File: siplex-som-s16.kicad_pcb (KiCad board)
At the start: 8 copper layers, 30 x 30 mm, 58 parts, among them J1 RFShield_OnePiece, J2 Conn_01x20, J3 Conn_01x20, J4 Conn_01x20, J6 Conn_01x20, U1 STM32H743IIKx, U2 IS42S16160J-6BLI, U3 W25Q32JVZP, U4 AP2112K-3.3, U5 W25Q32JVZP, Y1 25MHz, Y2 32.768KHz

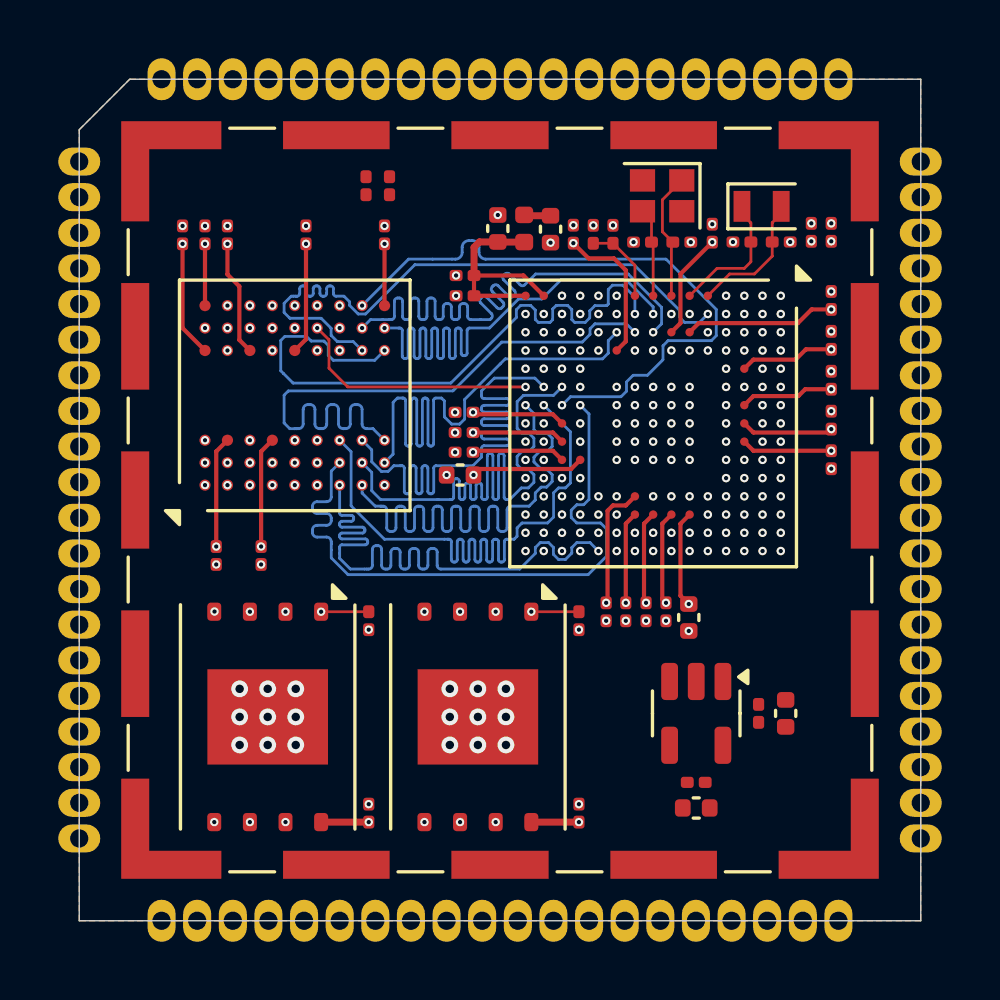
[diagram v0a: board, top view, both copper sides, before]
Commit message: Finished LTDC tracks
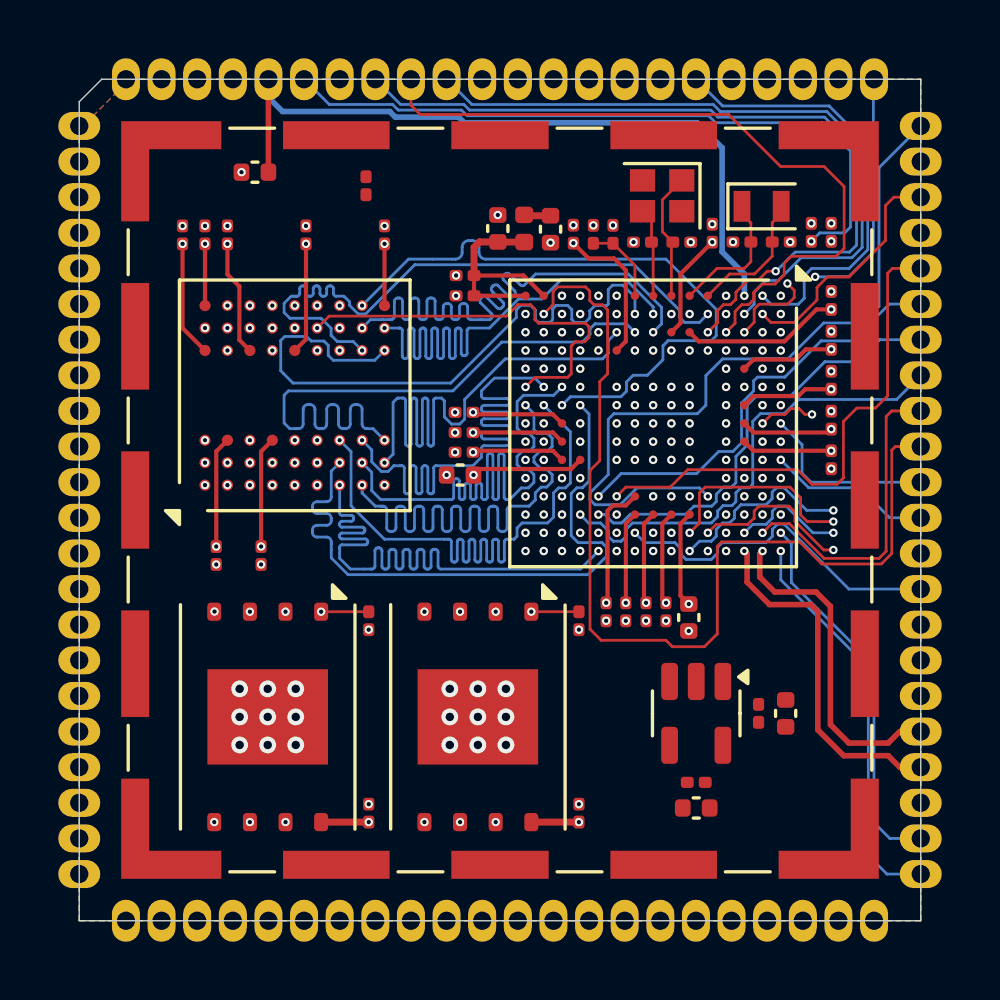
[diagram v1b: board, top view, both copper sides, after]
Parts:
- removed J2, J3, J4, J6: Conn_01x20, castellated_holes_header:castellated_01x20_P1.27mm
- added J5: Conn_01x22, castellated_holes_header:castellated_01x22_P1.27mm, F.Cu at (155.3, 111.4)
- added J7: Conn_01x22, castellated_holes_header:castellated_01x22_P1.27mm, F.Cu at (127.0, 83.1)
- added J8: Conn_01x22, castellated_holes_header:castellated_01x22_P1.27mm, F.Cu at (125.3, 84.7)
- added J9: Conn_01x22, castellated_holes_header:castellated_01x22_P1.27mm, F.Cu at (127.0, 113.1)
- C10: value 100n -> 10u; footprint Capacitor_SMD:C_0201_0603Metric -> Capacitor_SMD:C_0402_1005Metric
- moved C10 4.82 mm to (131.6, 86.4), turned to 180 degrees
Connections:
- C10 pad 1: GND -> VBAT
- C10 pad 2: +3V3 -> GND
- U1 pad A10: /MCU/SWO -> /Castellated_holes/SWO
- U1 pad A14: /MCU/SWCLK -> /Castellated_holes/SWCLK
- U1 pad A15: /MCU/SWDIO -> /Castellated_holes/SWDIO
- U1 pad A8: unconnected-(U1-PG13-PadA8) -> /Castellated_holes/LTDC_R0
- U1 pad A9: unconnected-(U1-PB4-PadA9) -> /Castellated_holes/SDMMC_IO3
- U1 pad B1: unconnected-(U1-PE4-PadB1) -> /Castellated_holes/LTDC_B0
- U1 pad B10: unconnected-(U1-PG10-PadB10) -> /Castellated_holes/LTDC_G3
- U1 pad B11: unconnected-(U1-PD6-PadB11) -> /Castellated_holes/SDMMC_CLK
- U1 pad B14: unconnected-(U1-PC10-PadB14) -> /Castellated_holes/LTDC_R2
- U1 pad B15: /MCU/USB_DP -> /Castellated_holes/USB_DP
- U1 pad B2: unconnected-(U1-PE5-PadB2) -> /Castellated_holes/LTDC_G0
- U1 pad B3: unconnected-(U1-PE6-PadB3) -> /Castellated_holes/LTDC_G1
- U1 pad B8: unconnected-(U1-PG12-PadB8) -> /Castellated_holes/LTDC_B1
- U1 pad B9: unconnected-(U1-PG11-PadB9) -> /Castellated_holes/SDMMC_IO2
- U1 pad C14: unconnected-(U1-PI2-PadC14) -> /Castellated_holes/LTDC_G7
- U1 pad C15: /MCU/USB_DN -> /Castellated_holes/USB_DN
- U1 pad C2: unconnected-(U1-PI7-PadC2) -> /Castellated_holes/LTDC_B7
- U1 pad C3: unconnected-(U1-PI6-PadC3) -> /Castellated_holes/LTDC_B6
- U1 pad C4: unconnected-(U1-PI5-PadC4) -> /Castellated_holes/LTDC_B5
- U1 pad D13: unconnected-(U1-PH15-PadD13) -> /Castellated_holes/LTDC_G4
- U1 pad D14: unconnected-(U1-PI1-PadD14) -> /Castellated_holes/LTDC_G6
- U1 pad D3: unconnected-(U1-PI9-PadD3) -> /Castellated_holes/LTDC_VSYNC
- U1 pad D4: unconnected-(U1-PI4-PadD4) -> /Castellated_holes/LTDC_B4
- U1 pad E12: unconnected-(U1-PH13-PadE12) -> /Castellated_holes/LTDC_G2
- U1 pad E14: unconnected-(U1-PI0-PadE14) -> /Castellated_holes/LTDC_G5
- U1 pad E15: /MCU/USB_VBUS_DET -> /Castellated_holes/USB_VBUS_DET
- U1 pad E3: unconnected-(U1-PI10-PadE3) -> /Castellated_holes/LTDC_HSYNC
- U1 pad F14: unconnected-(U1-PC9-PadF14) -> /Castellated_holes/LTDC_B2
- U1 pad F15: unconnected-(U1-PA8-PadF15) -> /Castellated_holes/LTDC_B3
- U1 pad J14: unconnected-(U1-PG7-PadJ14) -> /Castellated_holes/LTDC_CLK
- U1 pad J15: unconnected-(U1-PG6-PadJ15) -> /Castellated_holes/LTDC_R7
- U1 pad K12: unconnected-(U1-PH12-PadK12) -> /Castellated_holes/LTDC_R6
- U1 pad L1: unconnected-(U1-PF10-PadL1) -> /Castellated_holes/LTDC_DE
- U1 pad L12: unconnected-(U1-PH11-PadL12) -> /Castellated_holes/LTDC_R5
- U1 pad L13: unconnected-(U1-PH10-PadL13) -> /Castellated_holes/LTDC_R4
- U1 pad M13: unconnected-(U1-PH9-PadM13) -> /Castellated_holes/LTDC_R3
- U1 pad P2: unconnected-(U1-PA2-PadP2) -> /Castellated_holes/LTDC_R1
- U1 pad R14: unconnected-(U1-PB14-PadR14) -> /Castellated_holes/SDMMC_IO0
- U1 pad R15: unconnected-(U1-PB15-PadR15) -> /Castellated_holes/SDMMC_IO1
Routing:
- net /Castellated_holes/LTDC_R1: track 0.00 -> 34.8 mm, vias 0 -> 1
- net /Castellated_holes/LTDC_B2: track 0.00 -> 34.0 mm, vias 0 -> 2
- net /MCU/BOOT0: track 0.00 -> 32.7 mm
- net /Castellated_holes/LTDC_B3: track 0.00 -> 32.4 mm, vias 0 -> 2
- net /Castellated_holes/LTDC_HSYNC: track 0.00 -> 28.6 mm, vias 0 -> 2
- net /Castellated_holes/LTDC_G2: track 0.00 -> 26.8 mm, vias 0 -> 1
- net VBAT: track 0.00 -> 26.5 mm
- net /Castellated_holes/LTDC_VSYNC: track 0.00 -> 25.9 mm, vias 0 -> 1
- net /Castellated_holes/LTDC_G4: track 0.00 -> 25.1 mm, vias 0 -> 1
- net /Castellated_holes/LTDC_G5: track 0.00 -> 25.0 mm, vias 0 -> 2
- net /Castellated_holes/LTDC_B7: track 0.00 -> 24.8 mm, vias 0 -> 1
- net /Castellated_holes/LTDC_G7: track 0.00 -> 24.5 mm, vias 0 -> 2
- net /Castellated_holes/LTDC_G6: track 0.00 -> 23.7 mm, vias 0 -> 1
- net /Castellated_holes/LTDC_B5: track 0.00 -> 22.4 mm, vias 0 -> 1
- net /Castellated_holes/LTDC_B4: track 0.00 -> 22.2 mm, vias 0 -> 1
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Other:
- outline, holes or cut-outs redrawn

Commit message: test remote connection
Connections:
- U1 pad A11: unconnected-(U1-PD7-PadA11) -> /Castellated_holes/SDMMC_CMD
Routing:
- net unconnected-(U1-PE2-PadA2): track 0.00 -> 32.2 mm
- net unconnected-(U1-PE3-PadA1): track 0.00 -> 27.3 mm
- net /MCU/BOOT0: track 32.7 -> 34.0 mm
- net /Castellated_holes/LTDC_B0: track 16.0 -> 16.9 mm
- net /Castellated_holes/LTDC_B7: track 24.8 -> 25.8 mm
- net /Castellated_holes/LTDC_HSYNC: track 28.6 -> 29.5 mm
- net /Castellated_holes/LTDC_G1: track 10.5 -> 9.93 mm
- net unconnected-(U1-PD7-PadA11): vias 1 -> 0
- net /Castellated_holes/SDMMC_CMD: vias 0 -> 1
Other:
- board size 30 x 30 mm -> 31.6 x 31.6 mm

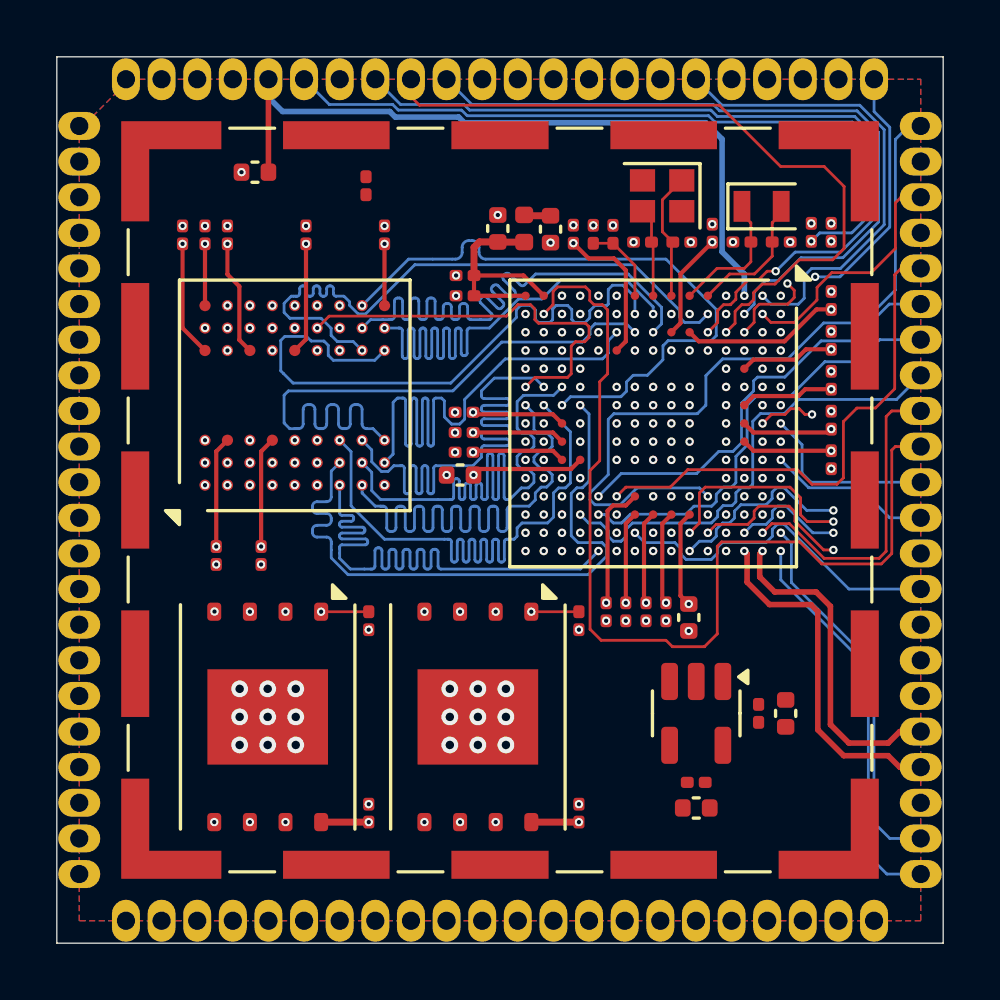
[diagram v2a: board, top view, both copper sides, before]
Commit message: Finished fanout all remaining pin, Power block left
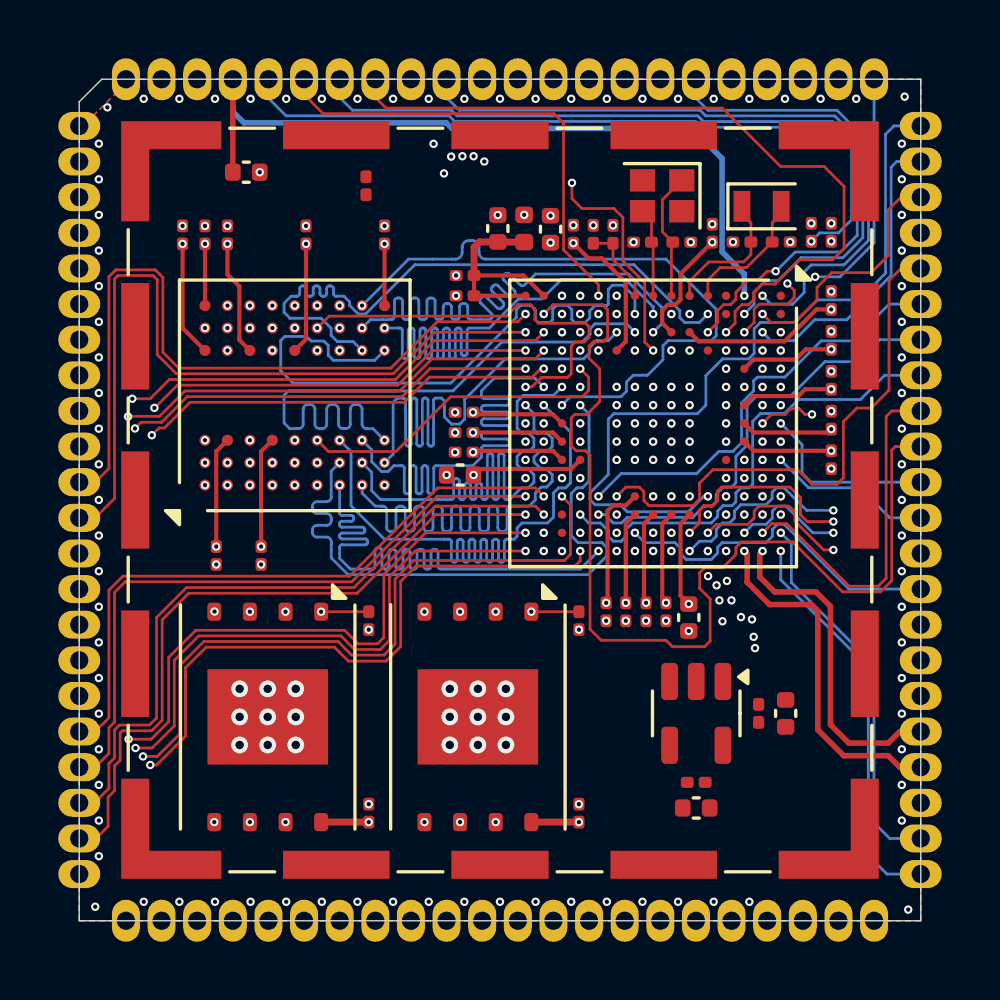
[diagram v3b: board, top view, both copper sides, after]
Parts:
- moved C10 0.31 mm to (131.3, 86.4), turned to 0 degrees
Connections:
- J7 pad 1: unconnected-(J7-Pin_1-Pad1) -> PB7
- J7 pad 2: unconnected-(J7-Pin_2-Pad2) -> PB5
- J7 pad 3: unconnected-(J7-Pin_3-Pad3) -> GND
- J7 pad 4: GND -> VBAT
- J7 pad 5: VBAT -> /MCU/BOOT0
- J7 pad 6: /MCU/BOOT0 -> /Castellated_holes/LTDC_DE
- J7 pad 7: /Castellated_holes/LTDC_DE -> /Castellated_holes/LTDC_HSYNC
- J7 pad 8: /Castellated_holes/LTDC_HSYNC -> /Castellated_holes/LTDC_VSYNC
- J7 pad 9: /Castellated_holes/LTDC_VSYNC -> GND
- J8 pad 1: unconnected-(J8-Pin_1-Pad1) -> PB8
- J8 pad 10: unconnected-(J8-Pin_10-Pad10) -> PA4
- J8 pad 11: unconnected-(J8-Pin_11-Pad11) -> PA3
- J8 pad 12: unconnected-(J8-Pin_12-Pad12) -> PA7
- J8 pad 13: unconnected-(J8-Pin_13-Pad13) -> PA6
- J8 pad 14: unconnected-(J8-Pin_14-Pad14) -> PA5
- J8 pad 15: unconnected-(J8-Pin_15-Pad15) -> PB0
- J8 pad 16: unconnected-(J8-Pin_16-Pad16) -> PB1
- J8 pad 17: unconnected-(J8-Pin_17-Pad17) -> PC5
- J8 pad 18: unconnected-(J8-Pin_18-Pad18) -> PB12
- J8 pad 19: unconnected-(J8-Pin_19-Pad19) -> PB10
- J8 pad 2: unconnected-(J8-Pin_2-Pad2) -> PB9
- J8 pad 20: unconnected-(J8-Pin_20-Pad20) -> PB13
- J8 pad 21: unconnected-(J8-Pin_21-Pad21) -> PB11
- J8 pad 22: unconnected-(J8-Pin_22-Pad22) -> PB14
- J8 pad 3: unconnected-(J8-Pin_3-Pad3) -> PH4
- J8 pad 4: unconnected-(J8-Pin_4-Pad4) -> GND
- J8 pad 5: unconnected-(J8-Pin_5-Pad5) -> PC0
- J8 pad 6: unconnected-(J8-Pin_6-Pad6) -> PC1
- J8 pad 7: unconnected-(J8-Pin_7-Pad7) -> PC4
- J8 pad 8: unconnected-(J8-Pin_8-Pad8) -> PA0
- J8 pad 9: unconnected-(J8-Pin_9-Pad9) -> PA1
- J9 pad 1: unconnected-(J9-Pin_1-Pad1) -> PB15
- J9 pad 10: unconnected-(J9-Pin_10-Pad10) -> PD3
- J9 pad 11: unconnected-(J9-Pin_11-Pad11) -> PD5
- J9 pad 12: unconnected-(J9-Pin_12-Pad12) -> PD6
- J9 pad 13: unconnected-(J9-Pin_13-Pad13) -> PD7
- J9 pad 14: unconnected-(J9-Pin_14-Pad14) -> PI3
- J9 pad 15: unconnected-(J9-Pin_15-Pad15) -> PA15
- J9 pad 16: unconnected-(J9-Pin_16-Pad16) -> PC12
- J9 pad 17: unconnected-(J9-Pin_17-Pad17) -> PG11
- J9 pad 18: unconnected-(J9-Pin_18-Pad18) -> PB4
- J9 pad 2: unconnected-(J9-Pin_2-Pad2) -> PH7
- J9 pad 3: unconnected-(J9-Pin_3-Pad3) -> PD13
- J9 pad 4: unconnected-(J9-Pin_4-Pad4) -> PC6
- J9 pad 5: unconnected-(J9-Pin_5-Pad5) -> PC7
- J9 pad 6: unconnected-(J9-Pin_6-Pad6) -> PC8
- J9 pad 7: unconnected-(J9-Pin_7-Pad7) -> PH14
- J9 pad 8: unconnected-(J9-Pin_8-Pad8) -> GND
- J9 pad 9: unconnected-(J9-Pin_9-Pad9) -> PD2
- U1 pad A1: unconnected-(U1-PE3-PadA1) -> PE3
- U1 pad A11: /Castellated_holes/SDMMC_CMD -> PD7
- U1 pad A12: unconnected-(U1-PC12-PadA12) -> PC12
- U1 pad A13: unconnected-(U1-PA15-PadA13) -> PA15
- U1 pad A2: unconnected-(U1-PE2-PadA2) -> PE2
- U1 pad A5: unconnected-(U1-PB8-PadA5) -> PB8
- U1 pad A6: unconnected-(U1-PB5-PadA6) -> PB5
- U1 pad A9: /Castellated_holes/SDMMC_IO3 -> PB4
- U1 pad B11: /Castellated_holes/SDMMC_CLK -> PD6
- U1 pad B4: unconnected-(U1-PB9-PadB4) -> PB9
- U1 pad B5: unconnected-(U1-PB7-PadB5) -> PB7
- U1 pad B9: /Castellated_holes/SDMMC_IO2 -> PG11
- U1 pad C11: unconnected-(U1-PD5-PadC11) -> PD5
- U1 pad C13: unconnected-(U1-PI3-PadC13) -> PI3
- U1 pad D1: unconnected-(U1-PC13-PadD1) -> PC13
- U1 pad D11: unconnected-(U1-PD3-PadD11) -> PD3
- U1 pad D12: unconnected-(U1-PD2-PadD12) -> PD2
- U1 pad D2: unconnected-(U1-PI8-PadD2) -> PI8
- U1 pad E13: unconnected-(U1-PH14-PadE13) -> PH14
- U1 pad E4: unconnected-(U1-PI11-PadE4) -> PI11
- U1 pad G14: unconnected-(U1-PC8-PadG14) -> PC8
- U1 pad G15: unconnected-(U1-PC7-PadG15) -> PC7
- U1 pad H15: unconnected-(U1-PC6-PadH15) -> PC6
- U1 pad H4: unconnected-(U1-PH4-PadH4) -> PH4
- U1 pad M15: unconnected-(U1-PD13-PadM15) -> PD13
- U1 pad M2: unconnected-(U1-PC0-PadM2) -> PC0
- U1 pad M3: unconnected-(U1-PC1-PadM3) -> PC1
- U1 pad N12: unconnected-(U1-PH7-PadN12) -> PH7
- U1 pad N2: unconnected-(U1-PA1-PadN2) -> PA1
- U1 pad N3: unconnected-(U1-PA0-PadN3) -> PA0
- U1 pad N4: unconnected-(U1-PA4-PadN4) -> PA4
- U1 pad N5: unconnected-(U1-PC4-PadN5) -> PC4
- U1 pad P12: unconnected-(U1-PB12-PadP12) -> PB12
- U1 pad P13: unconnected-(U1-PB13-PadP13) -> PB13
- U1 pad P3: unconnected-(U1-PA6-PadP3) -> PA6
- U1 pad P4: unconnected-(U1-PA5-PadP4) -> PA5
- U1 pad P5: unconnected-(U1-PC5-PadP5) -> PC5
- U1 pad R12: unconnected-(U1-PB10-PadR12) -> PB10
- U1 pad R13: unconnected-(U1-PB11-PadR13) -> PB11
- U1 pad R14: /Castellated_holes/SDMMC_IO0 -> PB14
- U1 pad R15: /Castellated_holes/SDMMC_IO1 -> PB15
- U1 pad R2: unconnected-(U1-PA3-PadR2) -> PA3
- U1 pad R3: unconnected-(U1-PA7-PadR3) -> PA7
- U1 pad R4: unconnected-(U1-PB1-PadR4) -> PB1
- U1 pad R5: unconnected-(U1-PB0-PadR5) -> PB0
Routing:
- net PB7: track 0.00 -> 39.4 mm, vias 0 -> 1
- net PB9: track 0.00 -> 38.9 mm, vias 0 -> 1
- net PB8: track 0.00 -> 38.4 mm, vias 0 -> 1
- net PB5: track 0.00 -> 38.1 mm, vias 0 -> 1
- net unconnected-(U1-PE2-PadA2): track 32.2 -> 0.00 mm, vias 1 -> 0
- net PA4: track 0.00 -> 30.7 mm, vias 0 -> 2
- net PH7: track 0.00 -> 30.7 mm, vias 0 -> 2
- net PD13: track 0.00 -> 29.9 mm, vias 0 -> 2
- net PA1: track 0.00 -> 29.9 mm, vias 0 -> 2
- net PC4: track 0.00 -> 29.2 mm, vias 0 -> 2
- net PA0: track 0.00 -> 29.2 mm, vias 0 -> 2
- net PC1: track 0.00 -> 28.6 mm, vias 0 -> 2
- net PH4: track 0.00 -> 28.0 mm, vias 0 -> 2
- net PA7: track 0.00 -> 27.7 mm, vias 0 -> 1
- net PC0: track 0.00 -> 27.7 mm, vias 0 -> 2
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- added copper zone on In3.Cu, net GND
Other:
- board size 31.6 x 31.6 mm -> 30 x 30 mm
